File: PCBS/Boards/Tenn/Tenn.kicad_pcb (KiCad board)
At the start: 2 copper layers, 90 x 25 mm, 29 parts, among them J1 Conn_01x02_Socket, J15 Conn_01x03_Male, J18 Conn_01x30_Pin, SW2 SW_Push, SW3 SW_Push, SW4 SW_SPDT, U2 DRV8871DDA, U3 DRV8871DDA

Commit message: updates PCB of tenn board
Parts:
- added G***: LOGO, LOGO, B.Cu at (178.8, 90.4)
- added G***: LOGO, LOGO, B.Cu at (166.1, 90.4)
- added G***: LOGO, LOGO, B.Cu at (138.2, 90.4)
- added G***: LOGO, LOGO, B.Cu at (130.5, 90.4)
- added G***: LOGO, LOGO, B.Cu at (133.0, 90.4)
- added G***: LOGO, LOGO, B.Cu at (158.5, 90.4)
- added G***: LOGO, LOGO, B.Cu at (122.9, 90.4)
- added G***: LOGO, LOGO, B.Cu at (163.5, 90.4)
- added G***: LOGO, LOGO, B.Cu at (143.2, 90.4)
- added G***: LOGO, LOGO, B.Cu at (173.8, 90.4)
- added G***: LOGO, LOGO, B.Cu at (148.3, 90.4)
- added G***: LOGO, LOGO, B.Cu at (140.6, 90.4)
- added G***: LOGO, LOGO, B.Cu at (171.2, 90.4)
- added G***: LOGO, LOGO, B.Cu at (120.3, 90.4)
- added G***: LOGO, LOGO, B.Cu at (128.0, 90.4)
- added G***: LOGO, LOGO, B.Cu at (145.8, 90.4)
- added G***: LOGO, LOGO, B.Cu at (161.1, 90.4)
- added G***: LOGO, LOGO, B.Cu at (155.9, 90.4)
- added G***: LOGO, LOGO, B.Cu at (168.7, 90.4)
- added G***: LOGO, LOGO, B.Cu at (181.3, 90.4)
- added G***: LOGO, LOGO, B.Cu at (150.8, 90.4)
- added G***: LOGO, LOGO, B.Cu at (125.4, 90.4)
- added G***: LOGO, LOGO, B.Cu at (135.6, 90.4)
- added G***: LOGO, LOGO, B.Cu at (117.8, 90.4)
- added G***: LOGO, LOGO, B.Cu at (153.4, 90.4)
- added G***: LOGO, LOGO, B.Cu at (176.3, 90.4)
- added G1: LOGO, LOGO, B.Cu at (107.6, 90.4)
- added G2: LOGO, LOGO, B.Cu at (110.2, 90.4)
- added G3: LOGO, LOGO, B.Cu at (112.7, 90.4)
- added G5: LOGO, LOGO, B.Cu at (115.3, 90.4)
- moved J15 34.0 mm to (138.1, 110.5)
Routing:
- net +5V: track 32.8 -> 169.6 mm, vias 0 -> 1
- net Sens0: track 0.00 -> 70.3 mm
- net Sens1: track 0.00 -> 65.3 mm
- net Sens2: track 0.00 -> 65.2 mm
- net MA1: track 0.00 -> 57.9 mm, vias 0 -> 1
- net MB2: track 0.00 -> 55.7 mm, vias 0 -> 1
- net GND: track 0.00 -> 55.3 mm, vias 0 -> 4
- net MB1: track 0.00 -> 48.8 mm, vias 0 -> 1
- net MA2: track 0.00 -> 46.2 mm, vias 0 -> 1
- net VCC: track 4.43 -> 48.1 mm
- net BTN2: track 4.15 -> 43.1 mm
- net SDA: track 0.00 -> 28.4 mm, vias 0 -> 2
- net Sens9: track 0.00 -> 25.9 mm
- net SCL: track 0.00 -> 24.9 mm, vias 0 -> 2
- net BTN1: track 4.15 -> 25.0 mm
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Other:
- board text added: "3.3V"
- board text added: "5V"
- board text added: "GND"

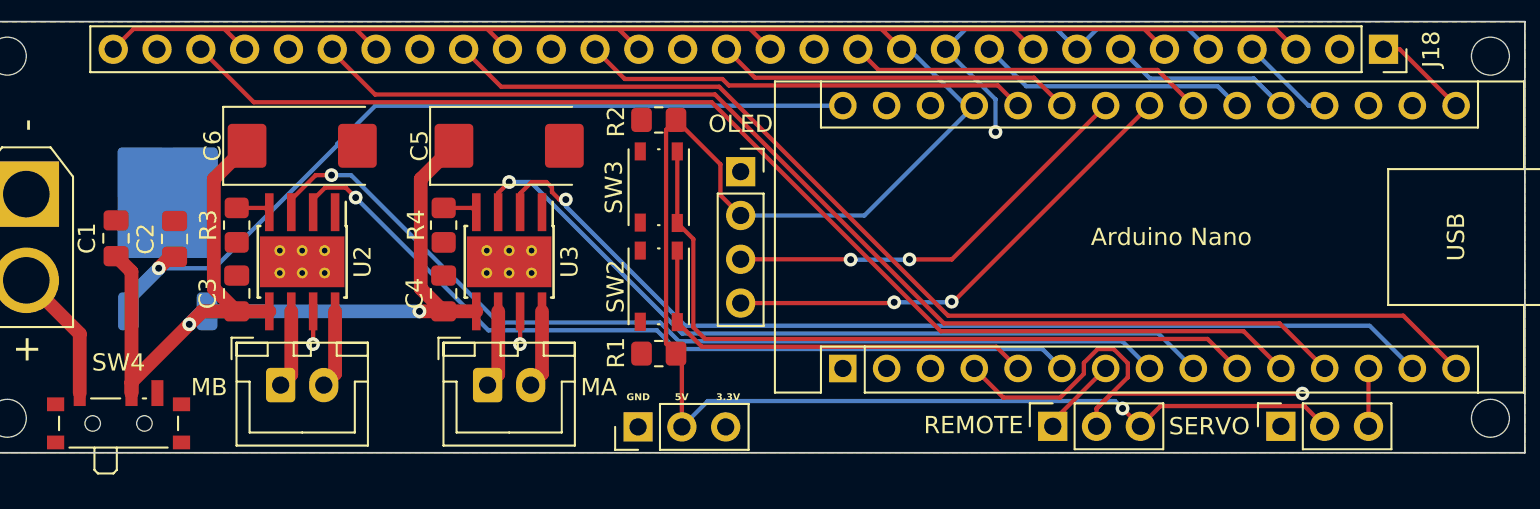
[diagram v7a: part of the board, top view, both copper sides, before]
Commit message: updates tenn board, adds gerber files, ready for production
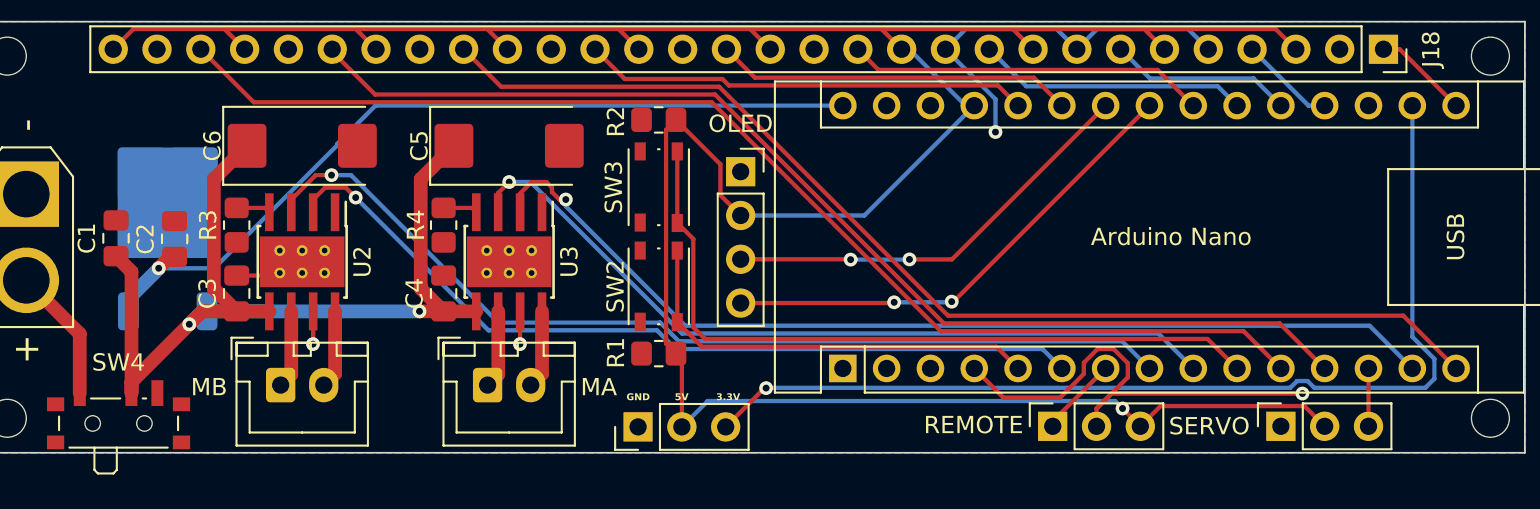
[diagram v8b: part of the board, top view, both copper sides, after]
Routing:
- net +3.3V: track 0.52 -> 59.5 mm, vias 0 -> 1
- net GND: track 55.3 -> 59.5 mm
